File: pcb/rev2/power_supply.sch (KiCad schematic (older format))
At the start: 48 parts, among them IC3 LV52204MUTBG, IC4 LM26480, IC5 TPS61040

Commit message: pcb wip
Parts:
- C41, C42, C43, C44, C45, C47, C48, C49, C51, C53, C55, C56, C57, C62, C63, C74, C78: footprint CAPC1608X87N -> Capacitors SMD:CAPC1608X87N
- C46, C50, C54, C58: footprint CAPC2012X135N -> Capacitors SMD:CAPC2012X135N
- C60, C61: footprint CAPMP3528X210N -> Capacitors SMD:CAPMP3528X210N
- D1, D2, D3, D4: footprint SOD3715X145N -> ICs And Semiconductors SMD:SOD3715X145N
- IC3: footprint (none) -> dsi_shield:UDFN6_2X2_065P
- IC4: footprint (none) -> ICs And Semiconductors SMD:QFN50P400X400X80-25N-S230
- IC5: footprint (none) -> ICs And Semiconductors SMD:SOT65P210X110-5N
- L2, L3, L4, L5: footprint (none) -> dsi_shield:IND_PANASONIC_ELLVEG
- R35, R36, R37, R38, R39, R40, R41, R42, R43, R44, R45, R46, R47, R53: footprint RESC1608X55N -> Resistors SMD:RESC1608X55N
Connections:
- net LCD_MVDRV renamed LCD_MVDD
- net LCD_PVDRV renamed LCD_PVDD

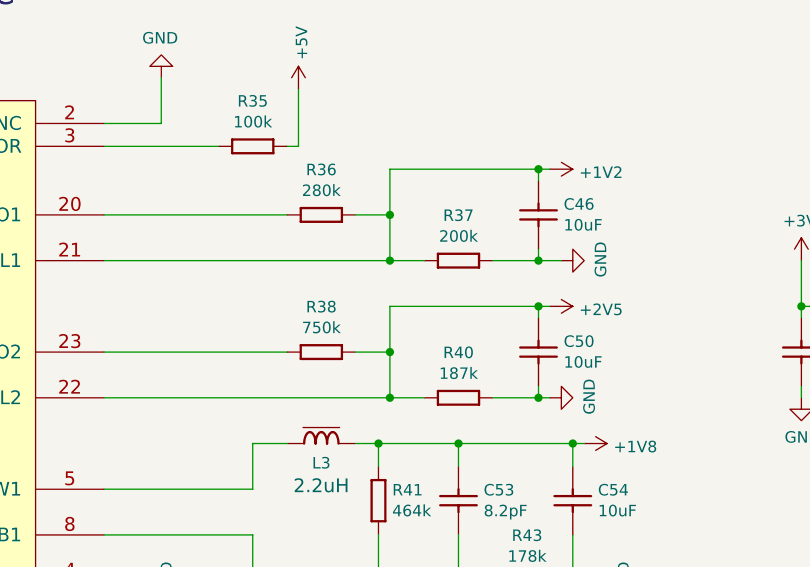
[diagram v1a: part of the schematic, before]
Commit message: Completed port to KiCad, passes DRC+LVS. NOT MANUFACTURED.
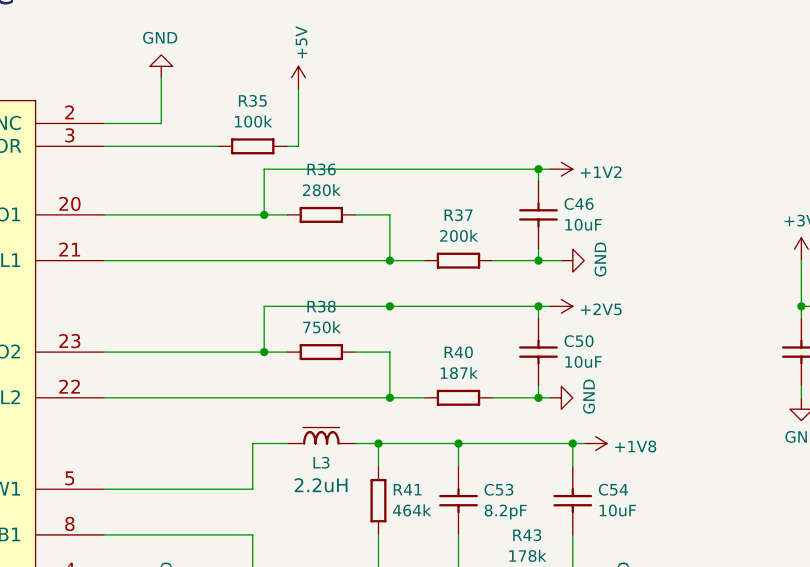
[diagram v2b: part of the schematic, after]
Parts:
- D1, D2, D3, D4: footprint ICs And Semiconductors SMD:SOD3715X145N -> ICs And Semiconductors SMD:SOD2713X115N
- IC5: footprint ICs And Semiconductors SMD:SOT65P210X110-5N -> ICs And Semiconductors SMD:SOT95P275X110-5N
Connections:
- net +1V2: now also IC4.20 (LDO1), R36.1; no longer IC4.21 (FBL1), R36.2, R37.1
- net +2V5: now also IC4.23 (LDO2), R38.1; no longer IC4.22 (FBL2), R38.2, R40.1
- new net: IC4.21 (FBL1), R36.2, R37.1
- new net: IC4.22 (FBL2), R38.2, R40.1
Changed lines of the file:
@@
 	3700 2000 5100 2000
-Wire Wire Line
-	4950 1600 4950 2000
 Wire Wire Line
 	4950 1800 4800 1800
 Connection ~ 4950 2000
 Wire Wire Line
-	4950 1600 5650 1600
-Connection ~ 4950 1800
+	4400 1600 5650 1600
 Wire Wire Line
 	5600 1650 5600 1600
@@
 Wire Wire Line
 	4800 2400 4950 2400
-Wire Wire Line
-	4950 2200 4950 2600
 Connection ~ 4950 2600
 Wire Wire Line
-	4950 2200 5650 2200
-Connection ~ 4950 2400
+	4400 2200 5650 2200
 Wire Wire Line
 	5400 2600 5650 2600
@@
 F 0 "IC5" H 7700 3065 50  0000 C CNN
 F 1 "TPS61040" H 7700 2010 60  0001 L CNN
-F 2 "ICs And Semiconductors SMD:SOT65P210X110-5N" H 7700 1920 60  0001 L CNN
+F 2 "ICs And Semiconductors SMD:SOT95P275X110-5N" H 7700 1920 60  0001 L CNN
 F 3 "" H 7700 1830 60  0001 L CNN
 F 4 "Value" H 7700 2500 60  0001 C CNN "Fieldname"
@@
 F 0 "D1" H 9500 1123 50  0000 C CNN
 F 1 "BAS170W" H 9500 1214 50  0000 C CNN
-F 2 "ICs And Semiconductors SMD:SOD3715X145N" H 9350 870 60  0001 L CNN
+F 2 "ICs And Semiconductors SMD:SOD2713X115N" H 9350 870 60  0001 L CNN
 F 3 "\\cern.ch\\dfs\\Applications\\Altium\\Datasheets\\MBR0530PBF.pdf" H 9350 780 60  0001 L CNN
 F 4 "Value" H 9350 1350 60  0001 C CNN "Fieldname"
@@
 F 0 "D2" V 9004 1540 50  0000 L CNN
 F 1 "BAS170W" V 9095 1540 50  0000 L CNN
-F 2 "ICs And Semiconductors SMD:SOD3715X145N" H 8900 970 60  0001 L CNN
+F 2 "ICs And Semiconductors SMD:SOD2713X115N" H 8900 970 60  0001 L CNN
 F 3 "\\cern.ch\\dfs\\Applications\\Altium\\Datasheets\\MBR0530PBF.pdf" H 8900 880 60  0001 L CNN
 F 4 "Value" H 8900 1450 60  0001 C CNN "Fieldname"
@@
 F 0 "D3" H 8550 2375 50  0000 C CNN
 F 1 "BAS170W" H 8675 2275 50  0000 C CNN
-F 2 "ICs And Semiconductors SMD:SOD3715X145N" H 8750 1720 60  0001 L CNN
+F 2 "ICs And Semiconductors SMD:SOD2713X115N" H 8750 1720 60  0001 L CNN
 F 3 "\\cern.ch\\dfs\\Applications\\Altium\\Datasheets\\MBR0530PBF.pdf" H 8750 1630 60  0001 L CNN
 F 4 "Value" H 8750 2200 60  0001 C CNN "Fieldname"
@@
 F 0 "D4" H 3650 6227 50  0000 C CNN
 F 1 "BAS170W" H 3650 6136 50  0000 C CNN
-F 2 "ICs And Semiconductors SMD:SOD3715X145N" H 3500 5520 60  0001 L CNN
+F 2 "ICs And Semiconductors SMD:SOD2713X115N" H 3500 5520 60  0001 L CNN
 F 3 "\\cern.ch\\dfs\\Applications\\Altium\\Datasheets\\MBR0530PBF.pdf" H 3500 5430 60  0001 L CNN
 F 4 "Value" H 3500 6000 60  0001 C CNN "Fieldname"
@@
 LCD_BOOST_FB
 $Comp
-L LCD_PVDD #PWR?
+L LCD_PVDD #PWR080
 U 1 1 599DF8B8
 P 9850 2200
-F 0 "#PWR?" H 9850 2050 50  0001 C CNN
+F 0 "#PWR080" H 9850 2050 50  0001 C CNN
 F 1 "LCD_PVDD" V 9865 2328 50  0000 L CNN
 F 2 "" H 9850 2200 50  0001 C CNN
@@
 $EndComp
 $Comp
-L LCD_MVDD #PWR?
+L LCD_MVDD #PWR081
 U 1 1 599DFBE9
 P 9850 1350
-F 0 "#PWR?" H 9850 1200 50  0001 C CNN
+F 0 "#PWR081" H 9850 1200 50  0001 C CNN
 F 1 "LCD_MVDD" V 9865 1478 50  0000 L CNN
 F 2 "" H 9850 1350 50  0001 C CNN
@@
 	0    1    1    0
 $EndComp
+Wire Wire Line
+	4950 1800 4950 2000
+Wire Wire Line
+	4400 1600 4400 1800
+Connection ~ 4400 1800
+Wire Wire Line
+	4400 2200 4400 2400
+Connection ~ 4400 2400
+Connection ~ 4950 2200
+Wire Wire Line
+	4950 2400 4950 2600
 $EndSCHEMATC

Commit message: axi4/zynq version: wip
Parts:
- C41, C42, C43, C44, C47, C48, C62, C63: symbol CC0603_1UF_50V_10%_X5R -> dsi_shield-rescue:CC0603_1UF_50V_10%_X5R-
- C45, C51, C55, C56: symbol CC0603_4.7UF_6.3V_10%_X5R -> dsi_shield-rescue:CC0603_4.7UF_6.3V_10%_X5R-
- C46, C50, C54, C58: symbol CC0805_10UF_16V_10%_X5R -> dsi_shield-rescue:CC0805_10UF_16V_10%_X5R-
- C49: symbol CC0603_22PF_50V_5%_NP0 -> dsi_shield-rescue:CC0603_22PF_50V_5%_NP0-
- C53: symbol CC0603_8.2PF_50V_0.5PF_NP0 -> dsi_shield-rescue:CC0603_8.2PF_50V_0.5PF_NP0-
- C57: symbol CC0603_6.8PF_50V_0.5PF_NP0 -> dsi_shield-rescue:CC0603_6.8PF_50V_0.5PF_NP0-
- C60, C61: symbol CTE3528-21_47UF_6.3V_10%_LESR0250 -> dsi_shield-rescue:CTE3528-21_47UF_6.3V_10%_LESR0250-
- C74: symbol CC0603_33PF_50V_5%_NP0 -> dsi_shield-rescue:CC0603_33PF_50V_5%_NP0-
- C78: symbol CC0603_220NF_10V_10%_X7R -> dsi_shield-rescue:CC0603_220NF_10V_10%_X7R-
- D1, D2, D3, D4: symbol Diode_Schottky -> dsi_shield-rescue:Diode_Schottky-
- IC3: symbol LV52204MUTBG -> dsi_shield-rescue:LV52204MUTBG-
- IC4: symbol LM26480 -> dsi_shield-rescue:LM26480-
- IC5: symbol TPS61041 -> dsi_shield-rescue:TPS61041-
- L2, L3, L4, L5: symbol DLCSM0315D-2R2-K -> dsi_shield-rescue:DLCSM0315D-2R2-K-
- R35, R39, R44, R46, R53: symbol R0603_100K_1%_0.1W_100PPM -> dsi_shield-rescue:R0603_100K_1%_0.1W_100PPM-
- R36, R40, R41, R43: symbol R0603_270K_1%_0.1W_100PPM -> dsi_shield-rescue:R0603_270K_1%_0.1W_100PPM-
- R37: symbol R0603_200K_1%_0.1W_100PPM -> dsi_shield-rescue:R0603_200K_1%_0.1W_100PPM-
- R38: symbol R0603_750K_1%_0.1W_100PPM -> dsi_shield-rescue:R0603_750K_1%_0.1W_100PPM-
- R42: symbol R0603_27K_1%_0.1W_100PPM -> dsi_shield-rescue:R0603_27K_1%_0.1W_100PPM-
- R45: symbol R0603_560K_1%_0.1W_100PPM -> dsi_shield-rescue:R0603_560K_1%_0.1W_100PPM-
- R47: symbol R0603_10R_1%_0.1W_200PPM -> dsi_shield-rescue:R0603_10R_1%_0.1W_200PPM-
